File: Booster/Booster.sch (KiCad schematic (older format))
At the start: 0 parts

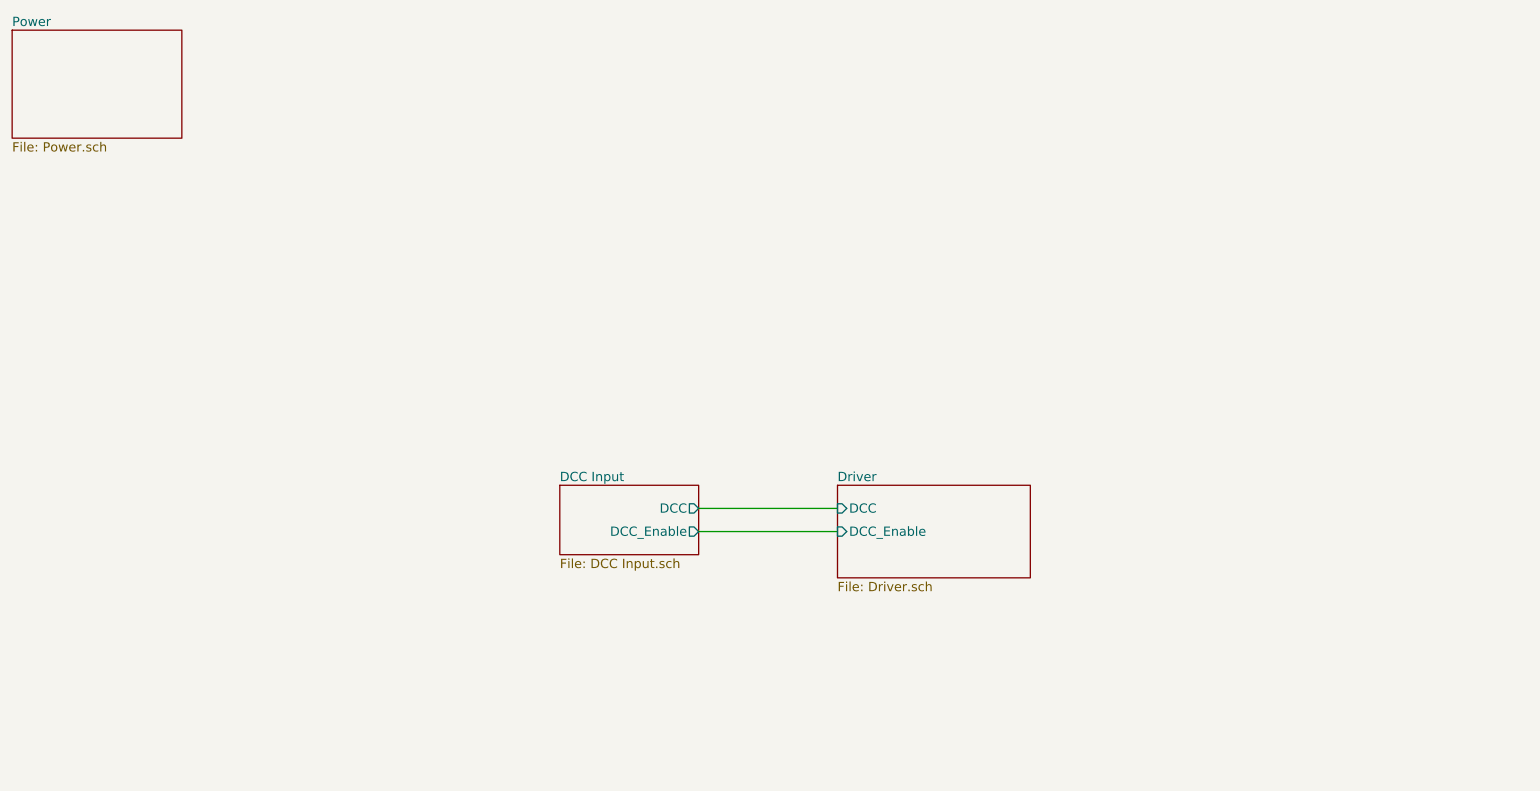
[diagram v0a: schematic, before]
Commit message: First draft of detecting overcurrent.
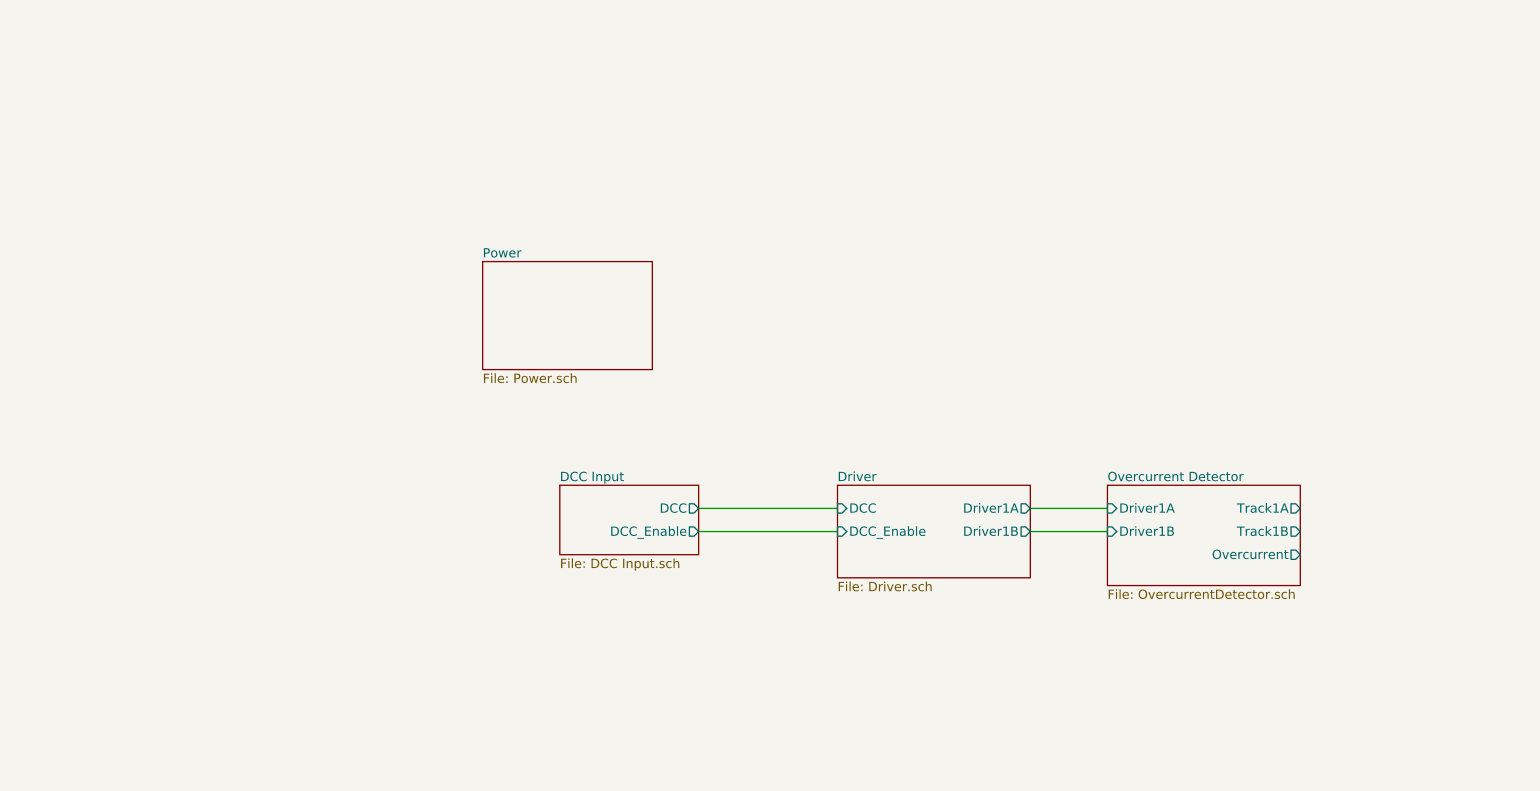
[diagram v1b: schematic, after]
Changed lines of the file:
@@
 $Descr A4 11693 8268
 encoding utf-8
-Sheet 1 4
+Sheet 1 5
 Title ""
 Date ""
@@
 $EndSheet
 $Sheet
-S 800  1000 1100 700
+S 3850 2500 1100 700
 U 59E9014C
 F0 "Power" 60
@@
 F2 "DCC_Enable" I L 6150 4250 60
 F3 "DCC" I L 6150 4100 60
+F4 "Driver1B" O R 7400 4250 60
+F5 "Driver1A" O R 7400 4100 60
 $EndSheet
 Wire Wire Line
@@
 Wire Wire Line
 	5250 4100 6150 4100
+$Sheet
+S 7900 3950 1250 650
+U 59ECA16F
+F0 "Overcurrent Detector" 60
+F1 "OvercurrentDetector.sch" 60
+F2 "Driver1A" I L 7900 4100 60
+F3 "Driver1B" I L 7900 4250 60
+F4 "Track1A" O R 9150 4100 60
+F5 "Track1B" O R 9150 4250 60
+F6 "Overcurrent" O R 9150 4400 60
+$EndSheet
+Wire Wire Line
+	7400 4250 7900 4250
+Wire Wire Line
+	7400 4100 7900 4100
 $EndSCHEMATC

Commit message: Trim pots to comparitors now set up to use fewer resistors. Added status sheet, currently not doing anything useful.
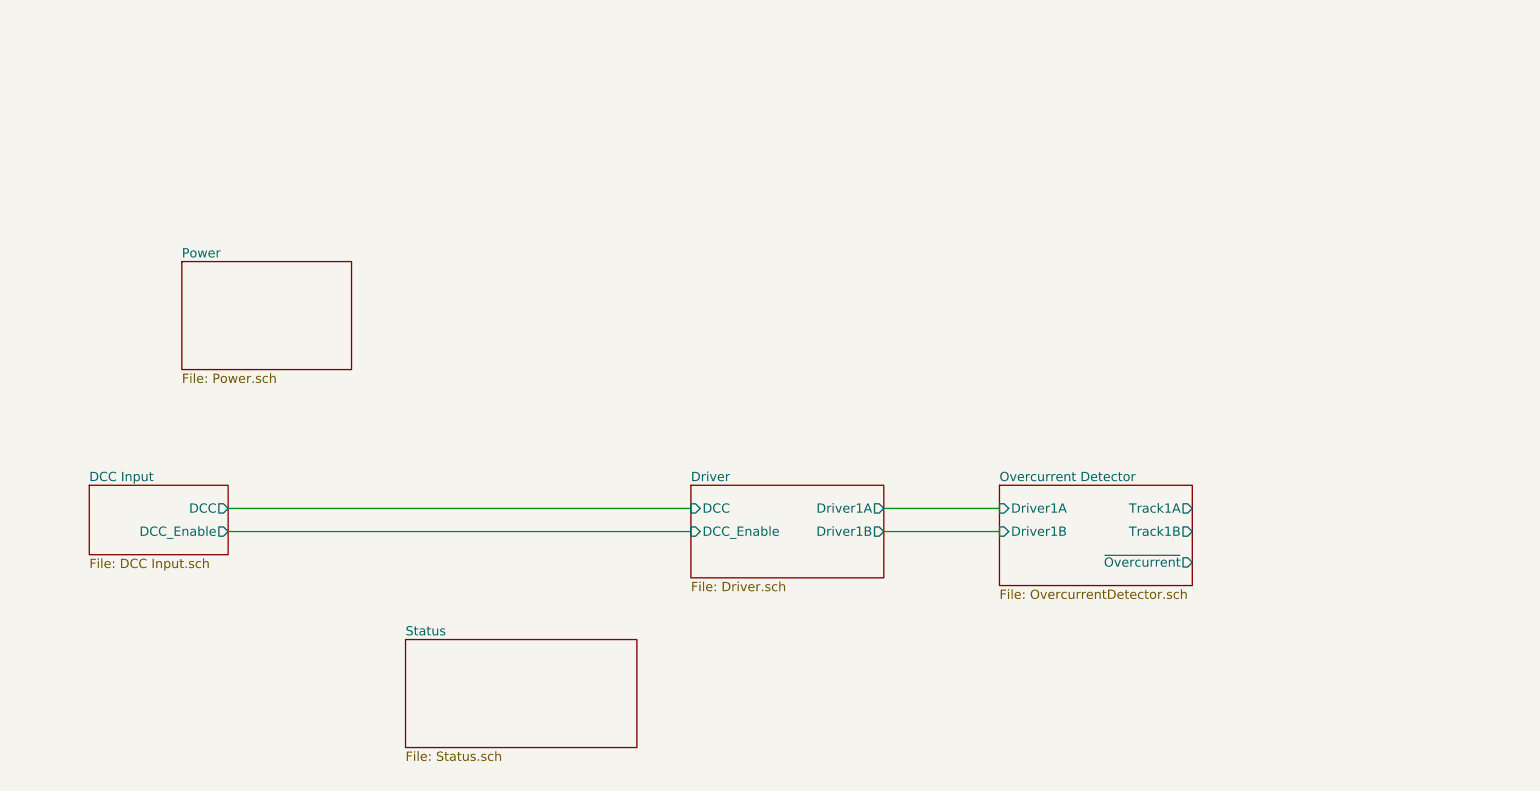
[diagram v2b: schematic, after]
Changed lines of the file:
@@
 $Descr A4 11693 8268
 encoding utf-8
-Sheet 1 5
+Sheet 1 6
 Title ""
 Date ""
@@
 $EndDescr
 $Sheet
-S 4350 3950 900  450
+S 1300 3950 900  450
 U 59E8EF77
 F0 "DCC Input" 60
 F1 "DCC Input.sch" 60
-F2 "DCC" O R 5250 4100 60
-F3 "DCC_Enable" O R 5250 4250 60
+F2 "DCC" O R 2200 4100 60
+F3 "DCC_Enable" O R 2200 4250 60
 $EndSheet
 $Sheet
-S 3850 2500 1100 700
+S 1900 2500 1100 700
 U 59E9014C
 F0 "Power" 60
@@
 $EndSheet
 $Sheet
-S 6150 3950 1250 600
+S 5200 3950 1250 600
 U 59E90CBD
 F0 "Driver" 60
 F1 "Driver.sch" 60
-F2 "DCC_Enable" I L 6150 4250 60
-F3 "DCC" I L 6150 4100 60
-F4 "Driver1B" O R 7400 4250 60
-F5 "Driver1A" O R 7400 4100 60
+F2 "DCC_Enable" I L 5200 4250 60
+F3 "DCC" I L 5200 4100 60
+F4 "Driver1B" O R 6450 4250 60
+F5 "Driver1A" O R 6450 4100 60
 $EndSheet
 Wire Wire Line
-	5250 4250 6150 4250
+	2200 4250 5200 4250
 Wire Wire Line
-	5250 4100 6150 4100
+	2200 4100 5200 4100
 $Sheet
-S 7900 3950 1250 650
+S 7200 3950 1250 650
 U 59ECA16F
 F0 "Overcurrent Detector" 60
 F1 "OvercurrentDetector.sch" 60
-F2 "Driver1A" I L 7900 4100 60
-F3 "Driver1B" I L 7900 4250 60
-F4 "Track1A" O R 9150 4100 60
-F5 "Track1B" O R 9150 4250 60
-F6 "Overcurrent" O R 9150 4400 60
+F2 "Driver1A" I L 7200 4100 60
+F3 "Driver1B" I L 7200 4250 60
+F4 "Track1A" O R 8450 4100 60
+F5 "Track1B" O R 8450 4250 60
+F6 "~Overcurrent" O R 8450 4450 60
 $EndSheet
 Wire Wire Line
-	7400 4250 7900 4250
+	6450 4250 7200 4250
 Wire Wire Line
-	7400 4100 7900 4100
+	6450 4100 7200 4100
+$Sheet
+S 3350 4950 1500 700
+U 59F0C14F
+F0 "Status" 60
+F1 "Status.sch" 60
+$EndSheet
 $EndSCHEMATC

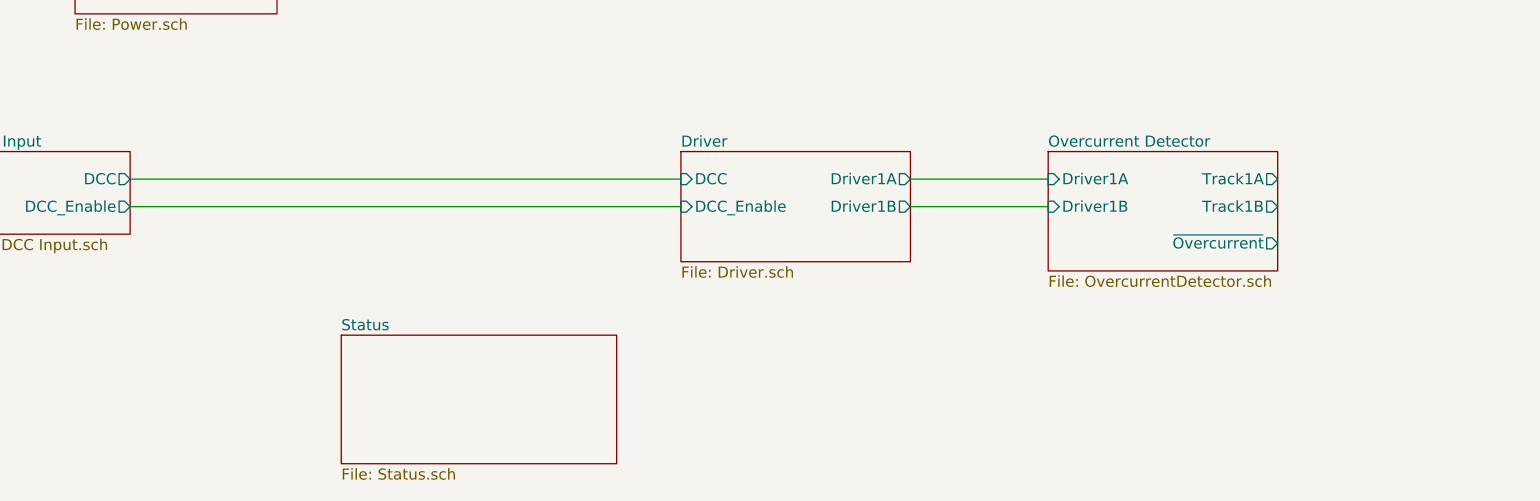
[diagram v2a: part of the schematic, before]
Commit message: Over current protection and detection - with detection delay and release delay.
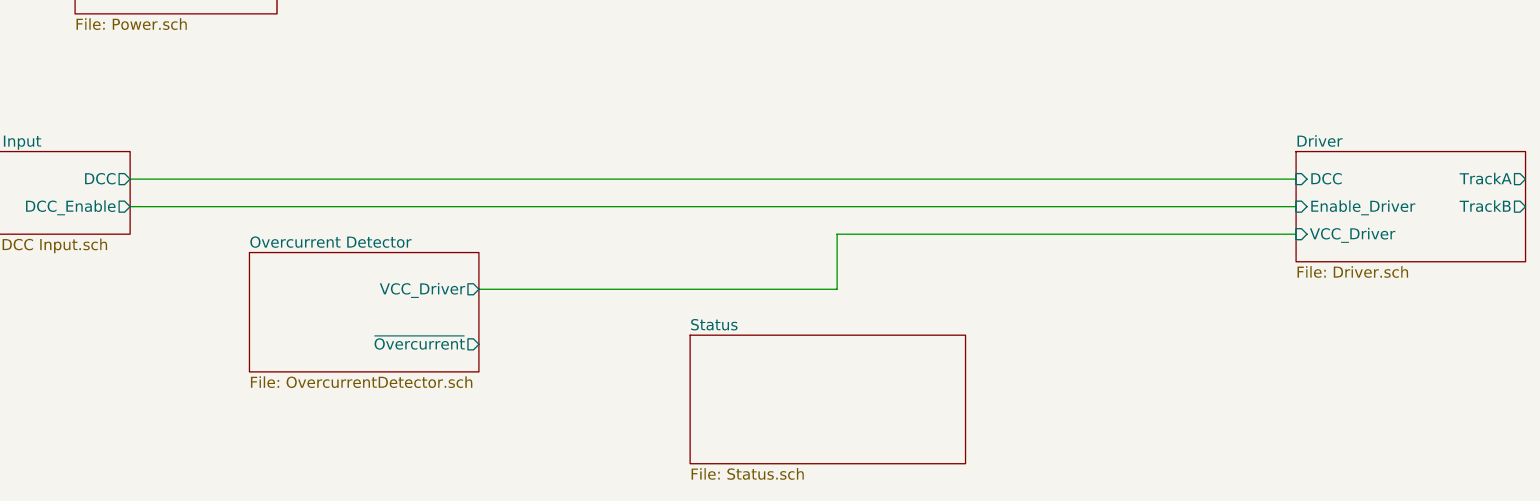
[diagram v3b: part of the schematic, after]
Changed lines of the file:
@@
 $EndSheet
 $Sheet
-S 5200 3950 1250 600
+S 8550 3950 1250 600
 U 59E90CBD
 F0 "Driver" 60
 F1 "Driver.sch" 60
-F2 "DCC_Enable" I L 5200 4250 60
-F3 "DCC" I L 5200 4100 60
-F4 "Driver1B" O R 6450 4250 60
-F5 "Driver1A" O R 6450 4100 60
+F2 "DCC" I L 8550 4100 60
+F3 "TrackA" O R 9800 4100 60
+F4 "TrackB" O R 9800 4250 60
+F5 "VCC_Driver" I L 8550 4400 60
+F6 "Enable_Driver" I L 8550 4250 60
 $EndSheet
 Wire Wire Line
-	2200 4250 5200 4250
+	2200 4250 8550 4250
 Wire Wire Line
-	2200 4100 5200 4100
+	2200 4100 8550 4100
 $Sheet
-S 7200 3950 1250 650
+S 2850 4500 1250 650
 U 59ECA16F
 F0 "Overcurrent Detector" 60
 F1 "OvercurrentDetector.sch" 60
-F2 "Driver1A" I L 7200 4100 60
-F3 "Driver1B" I L 7200 4250 60
-F4 "Track1A" O R 8450 4100 60
-F5 "Track1B" O R 8450 4250 60
-F6 "~Overcurrent" O R 8450 4450 60
+F2 "~Overcurrent" O R 4100 5000 60
+F3 "VCC_Driver" O R 4100 4700 60
 $EndSheet
-Wire Wire Line
-	6450 4250 7200 4250
-Wire Wire Line
-	6450 4100 7200 4100
 $Sheet
-S 3350 4950 1500 700
+S 5250 4950 1500 700
 U 59F0C14F
 F0 "Status" 60
 F1 "Status.sch" 60
 $EndSheet
+Wire Wire Line
+	4100 4700 6050 4700
+Wire Wire Line
+	6050 4700 6050 4400
+Wire Wire Line
+	6050 4400 8550 4400
 $EndSCHEMATC

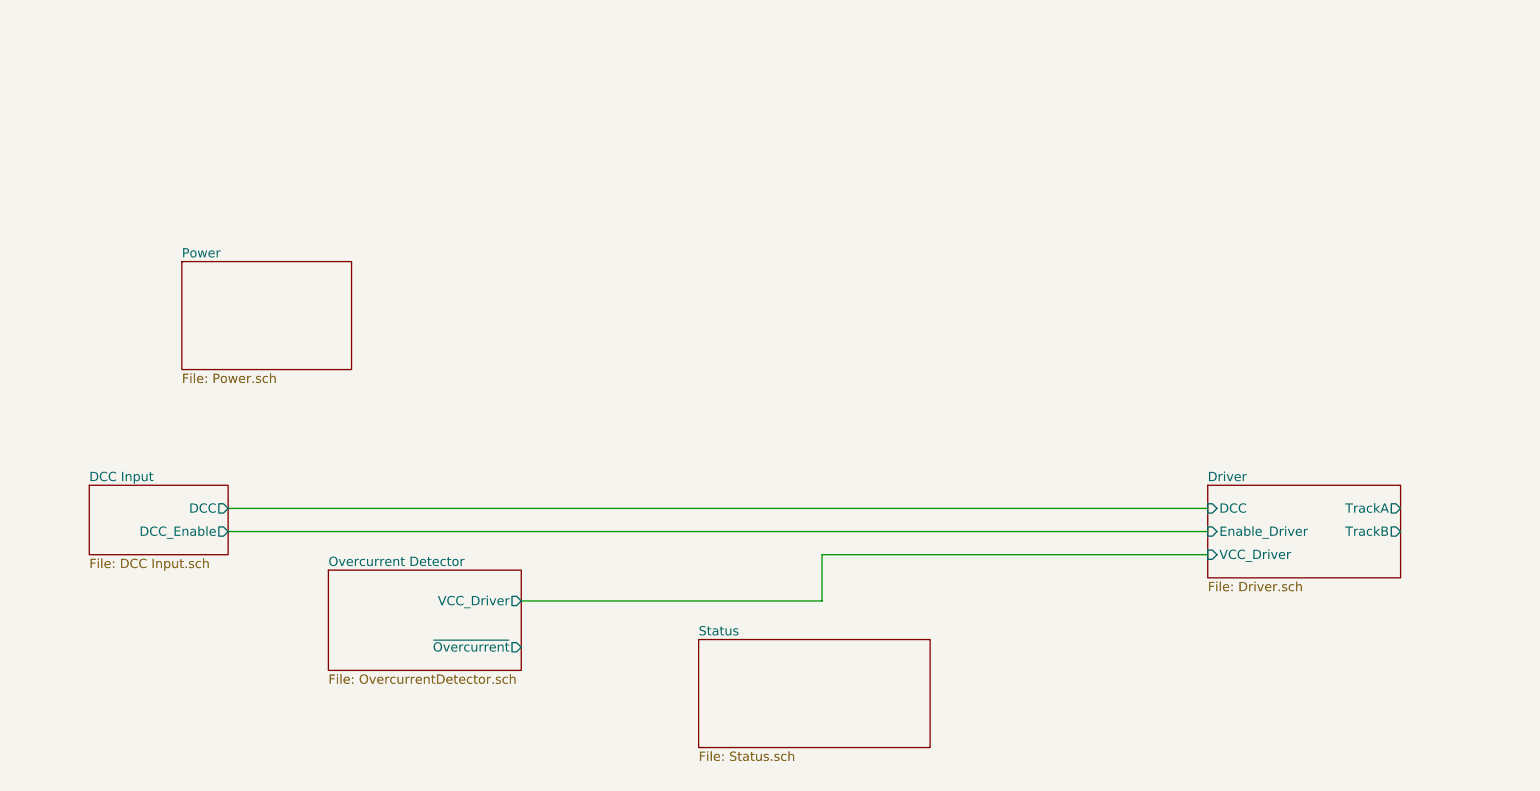
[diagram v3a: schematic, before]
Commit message: Added reversing support. Working on status output.
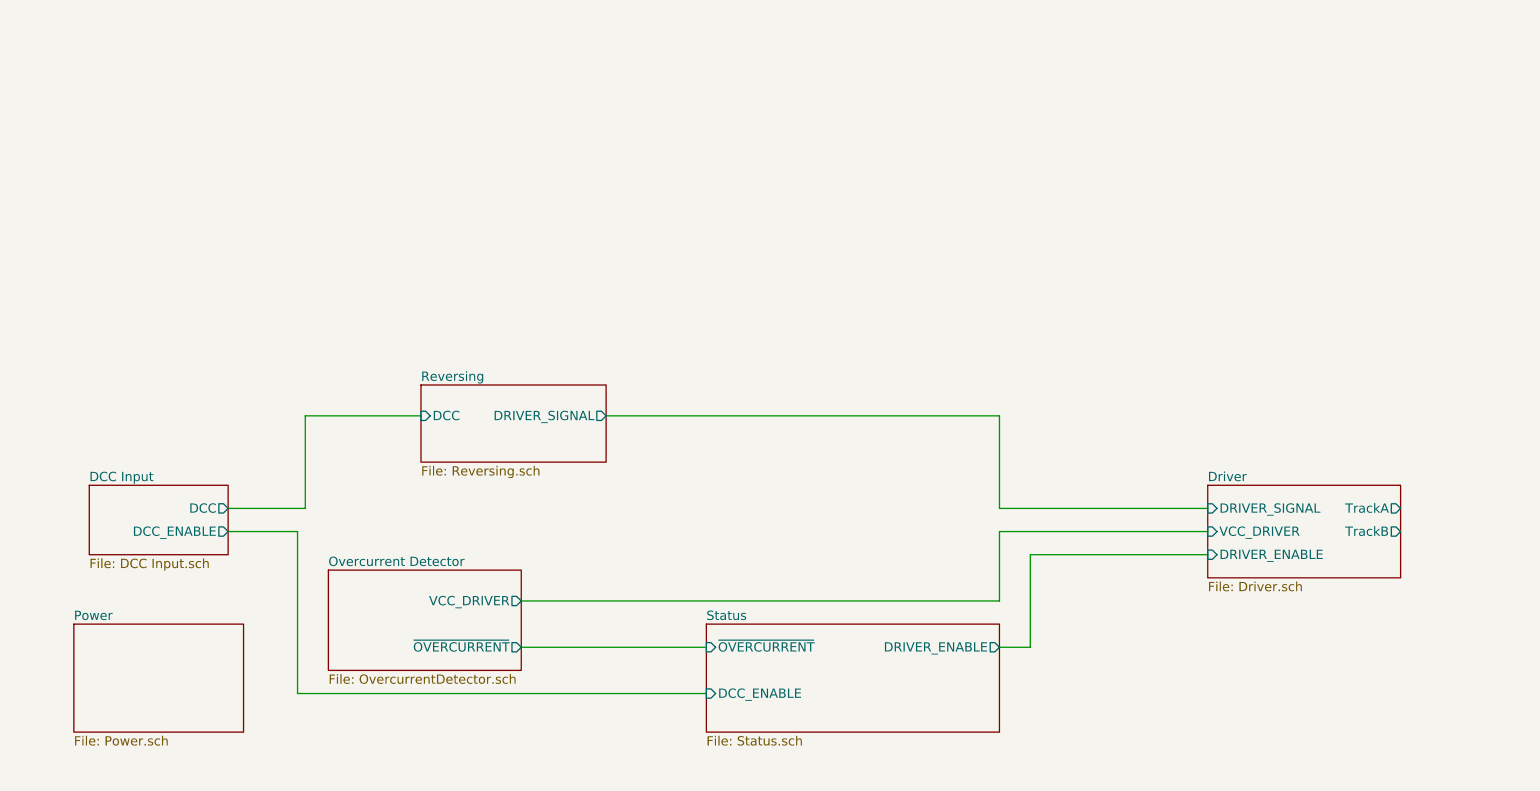
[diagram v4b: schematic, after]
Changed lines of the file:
@@
 $Descr A4 11693 8268
 encoding utf-8
-Sheet 1 6
+Sheet 1 7
 Title ""
 Date ""
@@
 F1 "DCC Input.sch" 60
 F2 "DCC" O R 2200 4100 60
-F3 "DCC_Enable" O R 2200 4250 60
+F3 "DCC_ENABLE" O R 2200 4250 60
 $EndSheet
 $Sheet
-S 1900 2500 1100 700
+S 1200 4850 1100 700
 U 59E9014C
 F0 "Power" 60
@@
 F0 "Driver" 60
 F1 "Driver.sch" 60
-F2 "DCC" I L 8550 4100 60
-F3 "TrackA" O R 9800 4100 60
-F4 "TrackB" O R 9800 4250 60
-F5 "VCC_Driver" I L 8550 4400 60
-F6 "Enable_Driver" I L 8550 4250 60
+F2 "TrackA" O R 9800 4100 60
+F3 "TrackB" O R 9800 4250 60
+F4 "DRIVER_ENABLE" I L 8550 4400 60
+F5 "DRIVER_SIGNAL" I L 8550 4100 60
+F6 "VCC_DRIVER" I L 8550 4250 60
 $EndSheet
-Wire Wire Line
-	2200 4250 8550 4250
-Wire Wire Line
-	2200 4100 8550 4100
 $Sheet
 S 2850 4500 1250 650
@@
 F0 "Overcurrent Detector" 60
 F1 "OvercurrentDetector.sch" 60
-F2 "~Overcurrent" O R 4100 5000 60
-F3 "VCC_Driver" O R 4100 4700 60
+F2 "~OVERCURRENT" O R 4100 5000 60
+F3 "VCC_DRIVER" O R 4100 4700 60
 $EndSheet
 $Sheet
-S 5250 4950 1500 700
+S 5300 4850 1900 700
 U 59F0C14F
 F0 "Status" 60
 F1 "Status.sch" 60
+F2 "DCC_ENABLE" I L 5300 5300 60
+F3 "~OVERCURRENT" I L 5300 5000 60
+F4 "DRIVER_ENABLE" O R 7200 5000 60
 $EndSheet
 Wire Wire Line
-	4100 4700 6050 4700
+	4100 4700 7200 4700
 Wire Wire Line
-	6050 4700 6050 4400
+	7200 4700 7200 4250
 Wire Wire Line
-	6050 4400 8550 4400
+	7200 4250 8550 4250
+$Sheet
+S 3450 3300 1200 500
+U 5A089893
+F0 "Reversing" 60
+F1 "Reversing.sch" 60
+F2 "DCC" I L 3450 3500 60
+F3 "DRIVER_SIGNAL" O R 4650 3500 60
+$EndSheet
+Wire Wire Line
+	2200 4100 2700 4100
+Wire Wire Line
+	2700 4100 2700 3500
+Wire Wire Line
+	2700 3500 3450 3500
+Wire Wire Line
+	4650 3500 7200 3500
+Wire Wire Line
+	7200 3500 7200 4100
+Wire Wire Line
+	7200 4100 8550 4100
+Wire Wire Line
+	2200 4250 2650 4250
+Wire Wire Line
+	2650 4250 2650 5300
+Wire Wire Line
+	2650 5300 5300 5300
+Wire Wire Line
+	4100 5000 5300 5000
+Wire Wire Line
+	7200 5000 7400 5000
+Wire Wire Line
+	7400 5000 7400 4400
+Wire Wire Line
+	7400 4400 8550 4400
 $EndSCHEMATC

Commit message: Getting close to feature complete for a single channel.
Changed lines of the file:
@@
 F0 "Overcurrent Detector" 60
 F1 "OvercurrentDetector.sch" 60
-F2 "~OVERCURRENT" O R 4100 5000 60
-F3 "VCC_DRIVER" O R 4100 4700 60
+F2 "VCC_DRIVER" O R 4100 4700 60
+F3 "OVERCURRENT" O R 4100 5000 60
 $EndSheet
 $Sheet
